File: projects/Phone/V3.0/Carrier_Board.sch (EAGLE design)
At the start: 4 parts, among them J1 3-1827231-6, J4 1-2199119-3, X1 PCI-E-164SOCKET

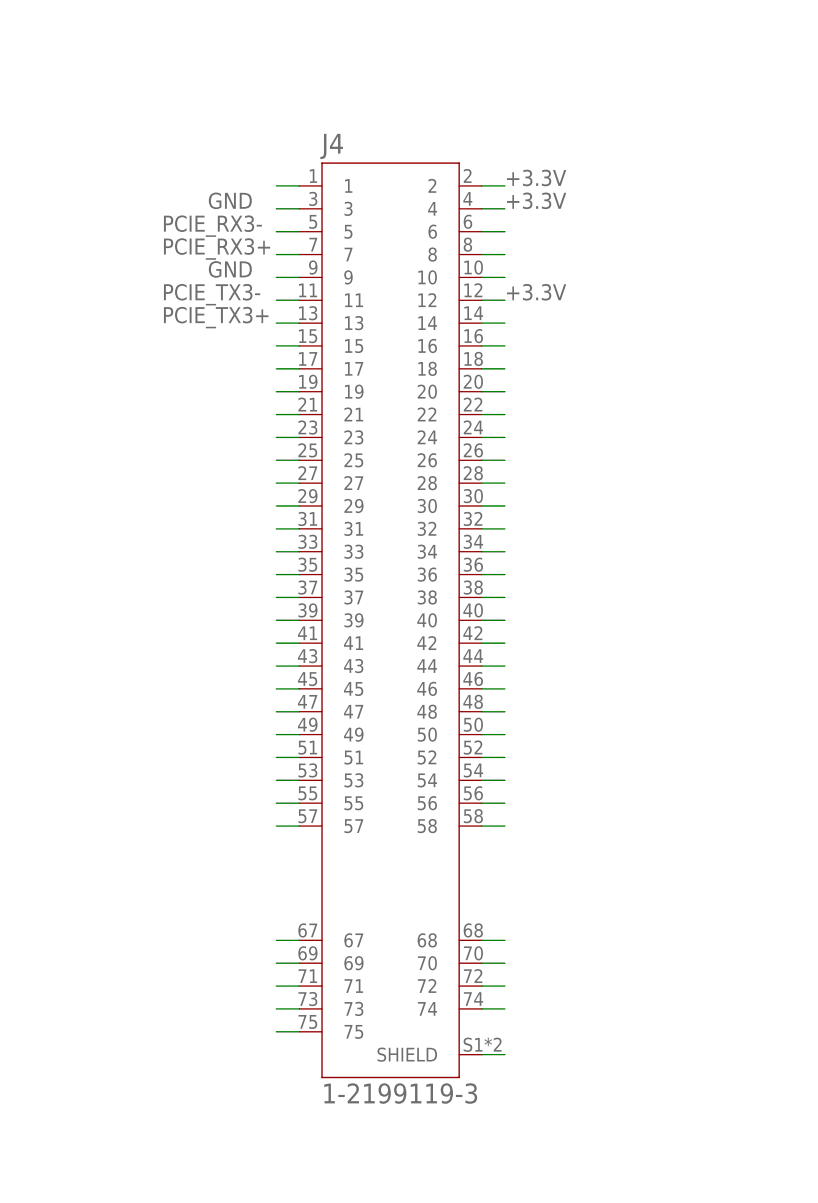
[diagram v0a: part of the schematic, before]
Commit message: populated m.2 schematic
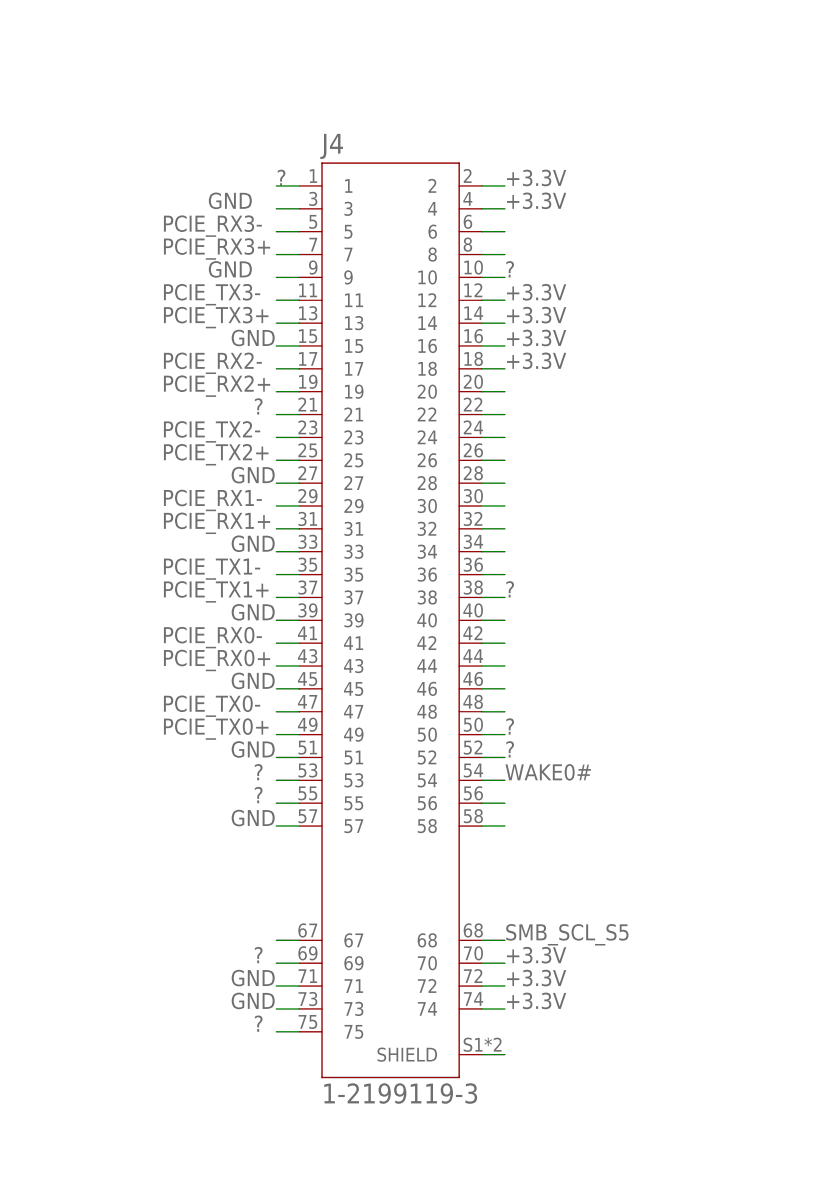
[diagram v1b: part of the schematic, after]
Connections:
- removed net N$1: J4.1
- removed net N$12: J4.15
- removed net N$13: J4.10
- removed net N$15: J4.14
- removed net N$16: J4.16
- removed net N$17: J4.17
- removed net N$18: J4.19
- removed net N$19: J4.21
- removed net N$20: J4.23
- removed net N$21: J4.18
- removed net N$26: J4.25
- removed net N$27: J4.27
- removed net N$29: J4.29
- removed net N$30: J4.31
- removed net N$35: J4.33
- removed net N$36: J4.35
- removed net N$37: J4.37
- removed net N$38: J4.39
- removed net N$41: J4.38
- removed net N$43: J4.41
- removed net N$44: J4.43
- removed net N$45: J4.45
- removed net N$46: J4.47
- removed net N$51: J4.49
- removed net N$52: J4.51
- removed net N$53: J4.53
- removed net N$54: J4.55
- removed net N$55: J4.50
- removed net N$56: J4.52
- removed net N$57: J4.54
- removed net N$58: J4.56
- removed net N$59: J4.57
- removed net N$61: J4.73
- removed net N$62: J4.74
- removed net N$63: J4.75
- removed net N$69: J4.69
- removed net N$70: J4.71
- removed net N$72: J4.68
- removed net N$73: J4.70
- removed net N$74: J4.72
- new net ?: J4.1, J4.10, J4.21, J4.38, J4.50, J4.52, J4.53, J4.55, J4.56, J4.69, J4.75
- net +3.3V: now also J4.14, J4.16, J4.18, J4.70, J4.72, J4.74
- net GND: now also J4.15, J4.27, J4.33, J4.39, J4.45, J4.51, J4.57, J4.71, J4.73
- net PCIE_RX0+: now also J4.43
- net PCIE_RX0-: now also J4.41
- net PCIE_RX1+: now also J4.31
- net PCIE_RX1-: now also J4.29
- net PCIE_RX2+: now also J4.19
- net PCIE_RX2-: now also J4.17
- net PCIE_TX0+: now also J4.49
- net PCIE_TX0-: now also J4.47
- net PCIE_TX1+: now also J4.37
- net PCIE_TX1-: now also J4.35
- net PCIE_TX2+: now also J4.25
- net PCIE_TX2-: now also J4.23
- net SMB_SCL_S5: now also J4.68
- net WAKE0#: now also J4.54

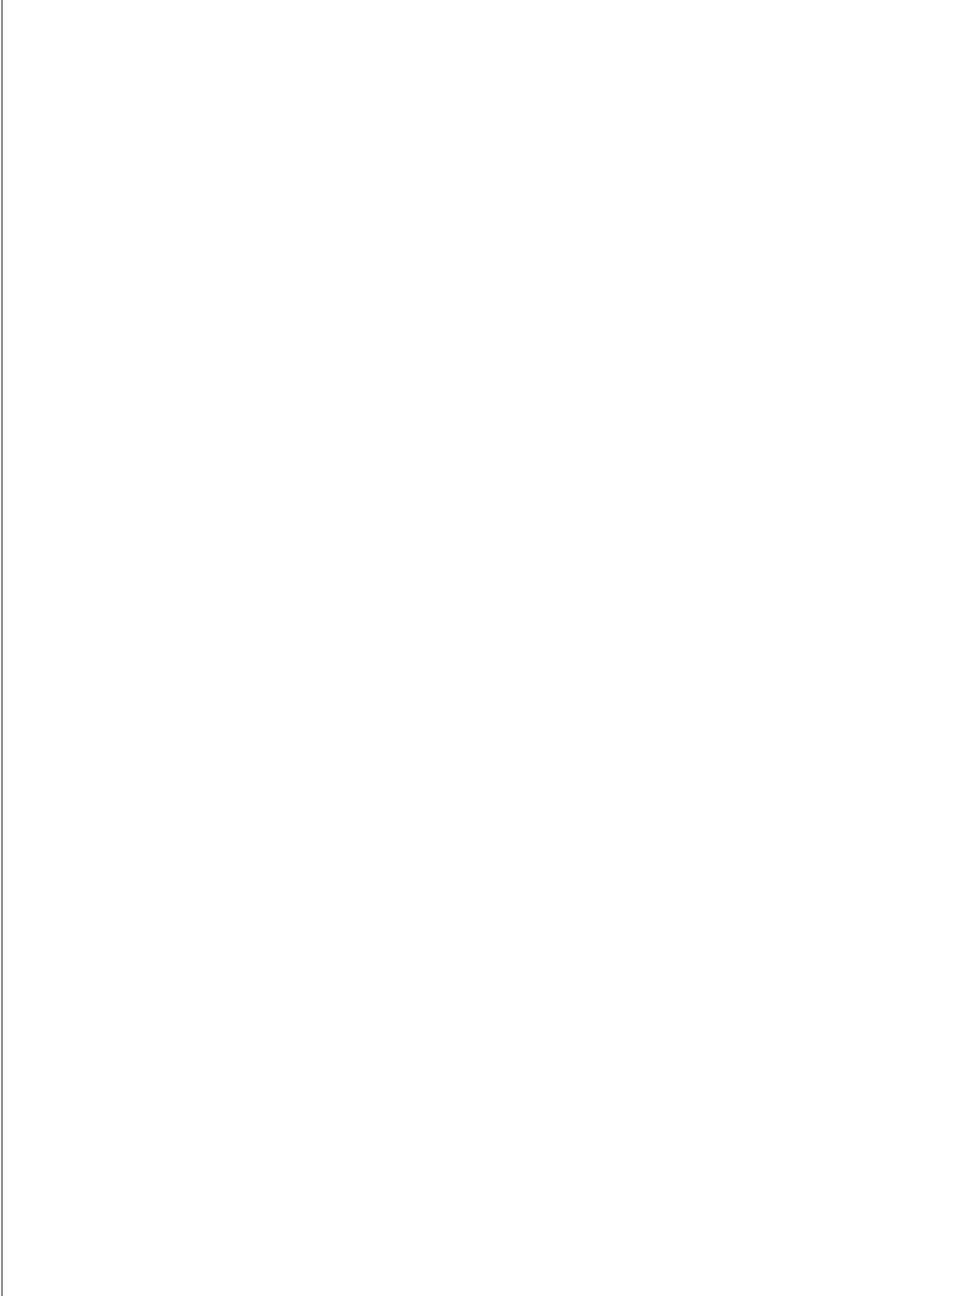
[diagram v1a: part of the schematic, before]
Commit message: added m.2 port for gsm
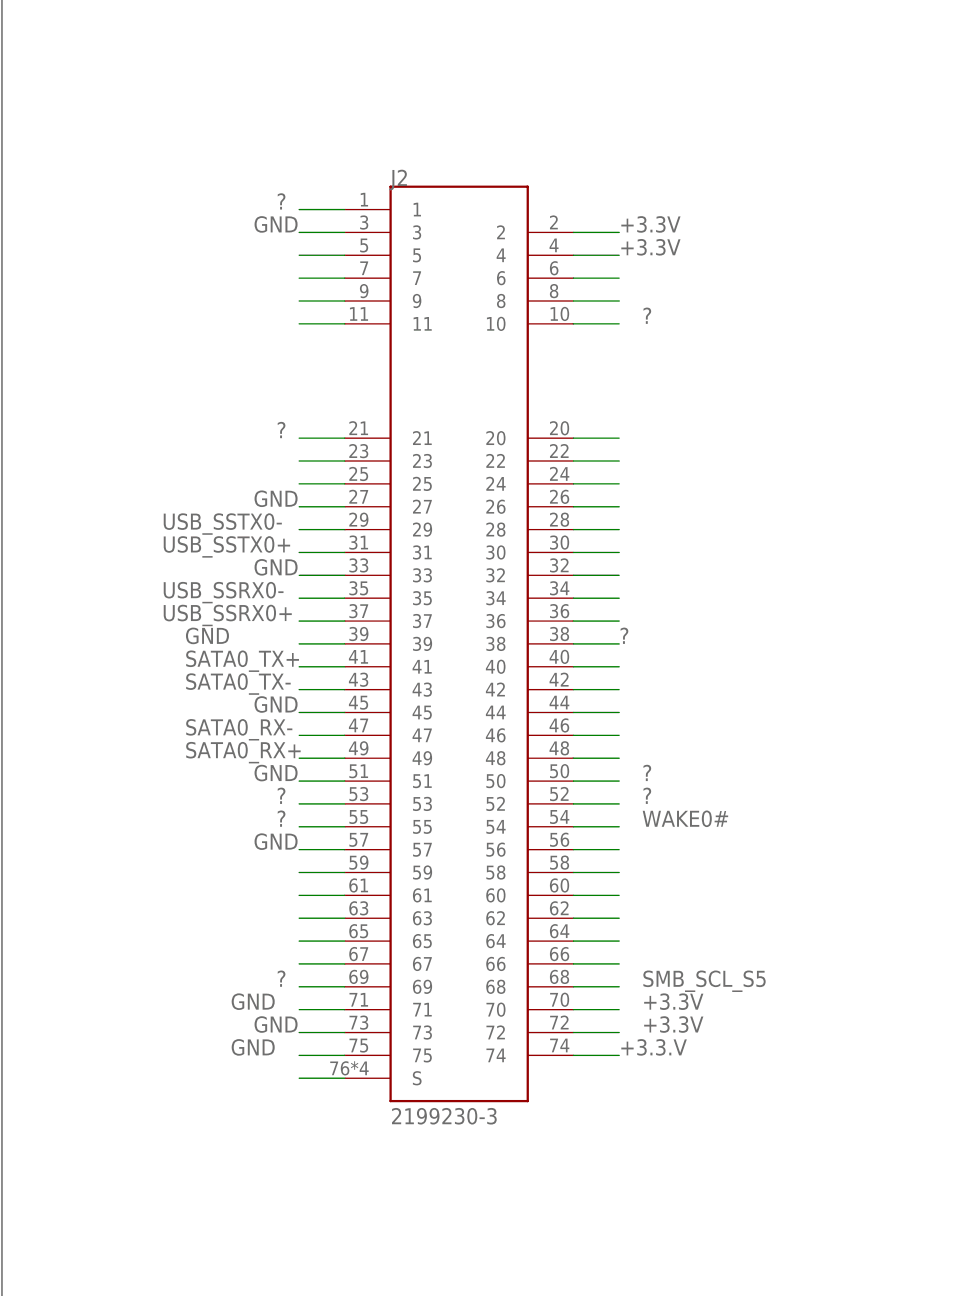
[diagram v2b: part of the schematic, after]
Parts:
- added J2: 2199230-3, 2199230-3:2199230-3
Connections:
- new net +3.3.V: J2.74
- new net N$12: J2.6
- new net N$13: J2.8
- new net N$15: J2.23
- new net N$16: J2.25
- new net N$20: J2.20
- new net N$21: J2.22
- new net N$26: J2.24
- new net N$27: J2.26
- new net N$29: J2.28
- new net N$30: J2.30
- new net N$4: J2.7
- new net N$44: J2.32
- new net N$45: J2.34
- new net N$46: J2.36
- new net N$5: J2.9
- new net N$52: J2.40
- new net N$53: J2.42
- new net N$6: J2.11
- new net N$61: J2.44
- new net N$62: J2.46
- new net N$63: J2.48
- new net N$70: J2.59
- new net N$71: J2.61
- new net N$72: J2.63
- new net N$73: J2.65
- new net N$74: J2.67
- new net N$75: J2.56
- new net N$76: J2.58
- new net N$77: J2.60
- new net N$78: J2.62
- new net N$79: J2.64
- new net N$80: J2.66
- new net N$85: J2.S
- new net USB_SSTX0-: J2.29
- net +3.3V: now also J2.2, J2.4, J2.70, J2.72
- net ?: now also J2.1, J2.10, J2.21, J2.38, J2.50, J2.52, J2.53, J2.55, J2.69
- net GND: now also J2.27, J2.3, J2.33, J2.39, J2.45, J2.51, J2.57, J2.71, J2.73, J2.75
- net SATA0_RX+: now also J2.49
- net SATA0_RX-: now also J2.47
- net SATA0_TX+: now also J2.41
- net SATA0_TX-: now also J2.43
- net SMB_SCL_S5: now also J2.68
- net USB_SSRX0+: now also J2.37
- net USB_SSRX0-: now also J2.35
- net USB_SSTX0+: now also J2.31, J2.5
- net WAKE0#: now also J2.54
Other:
- note added: "Check connections and mark unclear ones"
- note added: "Use m.2 GSM from sierra wireless over the usb protocol"
- note added: "Wifi is on chipset and bluetooth might be"
- note added: "figure out what to do about ? connections"

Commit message: asd
asd
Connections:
- net N$80 renamed SIM_DETECT
- removed net N$30: J2.30
- removed net N$4: J2.7
- removed net N$44: J2.32
- removed net N$45: J2.34
- removed net N$46: J2.36
- removed net N$5: J2.9
- new net N$11: J3.VPP
- new net N$17: J3.RFU1
- new net N$18: J3.DETECTION
- new net N$19: J3.COMMON
- new net N$9: J3.RFU
- new net UIM1_CLK: J2.32, J3.CLK
- new net UIM1_DATA: J2.34, J3.I/O
- new net UIM1_PWR: J2.36, J3.VCC
- new net UIM1_RESET: J2.30, J3.RST
- net ?: no longer J2.1, J2.10, J2.21, J2.69
- net GND: now also J2.21, J2.69, J3.GND; no longer J2.75
- net USB0+: now also J2.7
- net USB0-: now also J2.9
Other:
- note added: "3.5mm jack"
- note added: "Add current smothing caps and esd protection"
- note added: "Take input power from thunderbolt 3 then add battery charge circuit and 9-19v input to vcc to power everything else"
- note added: "add sata"
- note added: "eDP 1.4 (display port)"
- note added: "ethernet"
- note added: "hdmi"
- note added: "usb 3.1"
- note removed: "Audio"
- moved on the sheet: J2, J3
